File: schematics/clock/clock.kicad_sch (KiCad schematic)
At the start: 0 parts

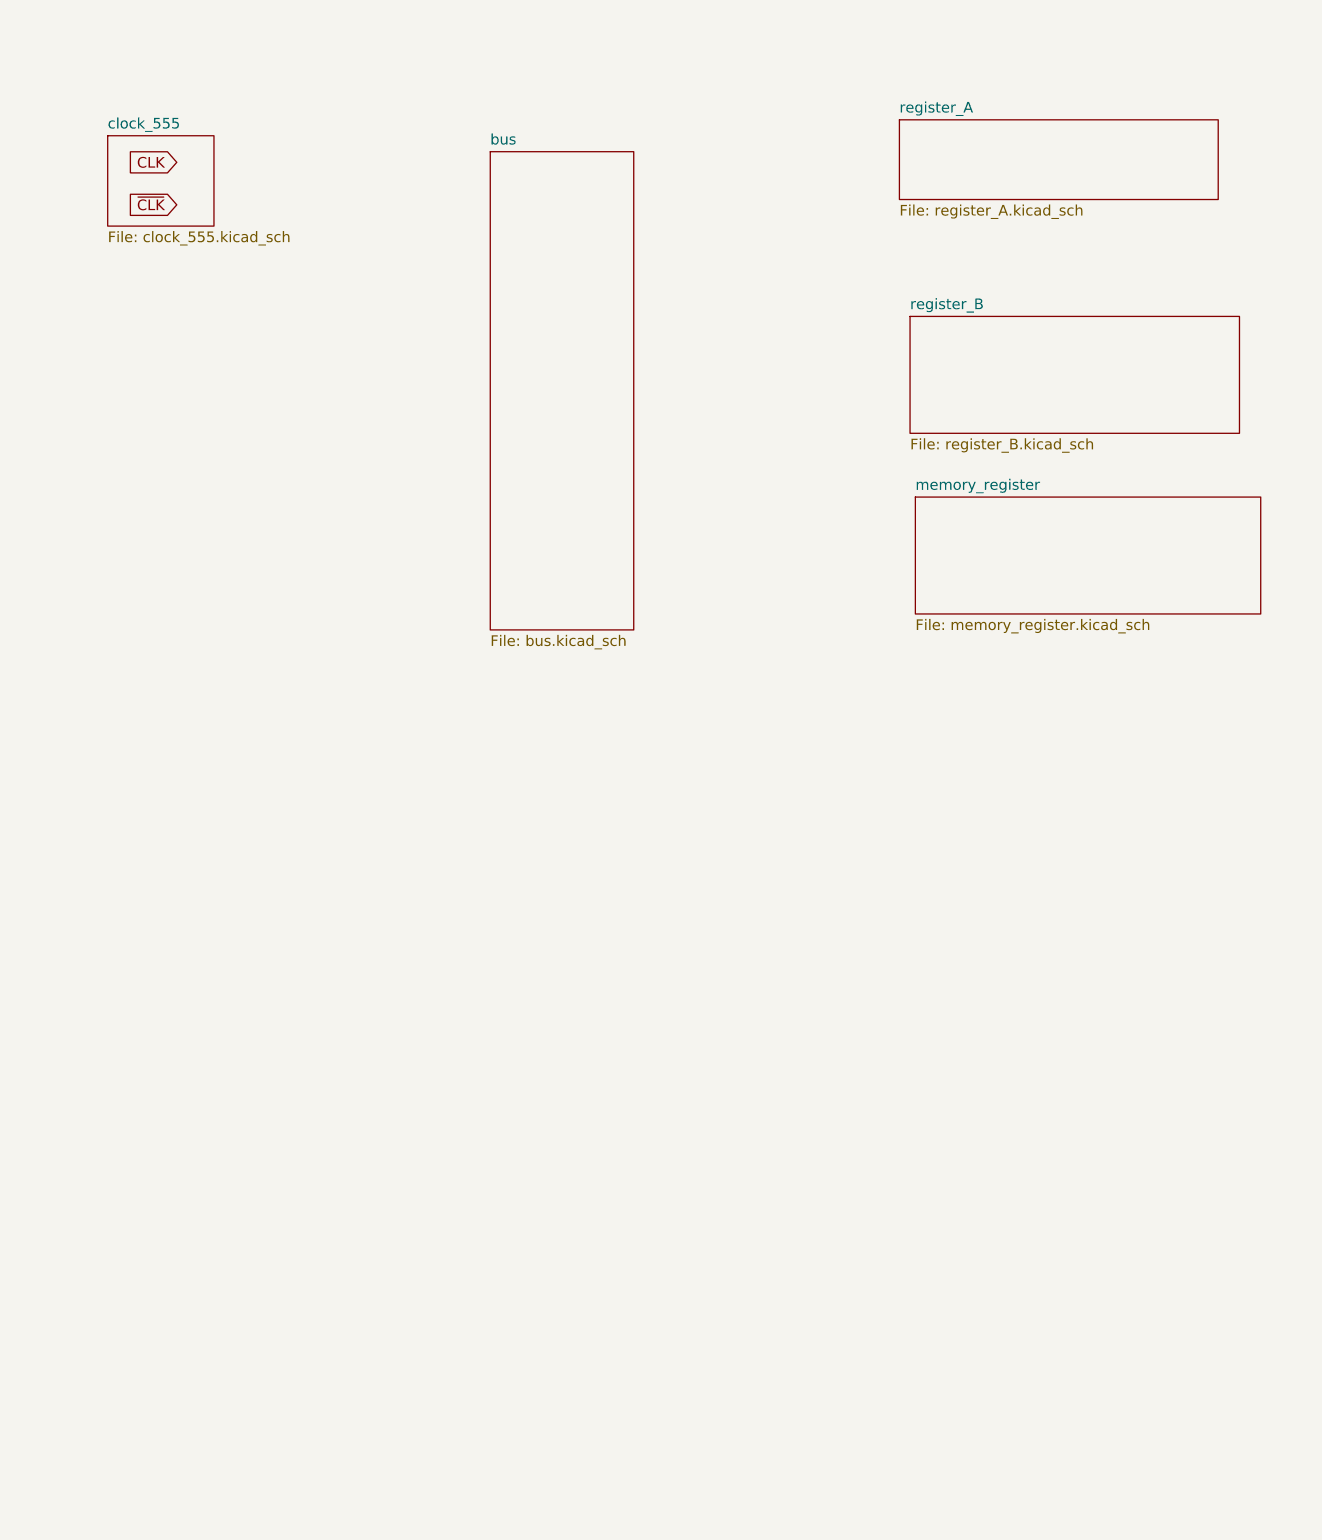
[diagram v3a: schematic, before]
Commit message: add bus
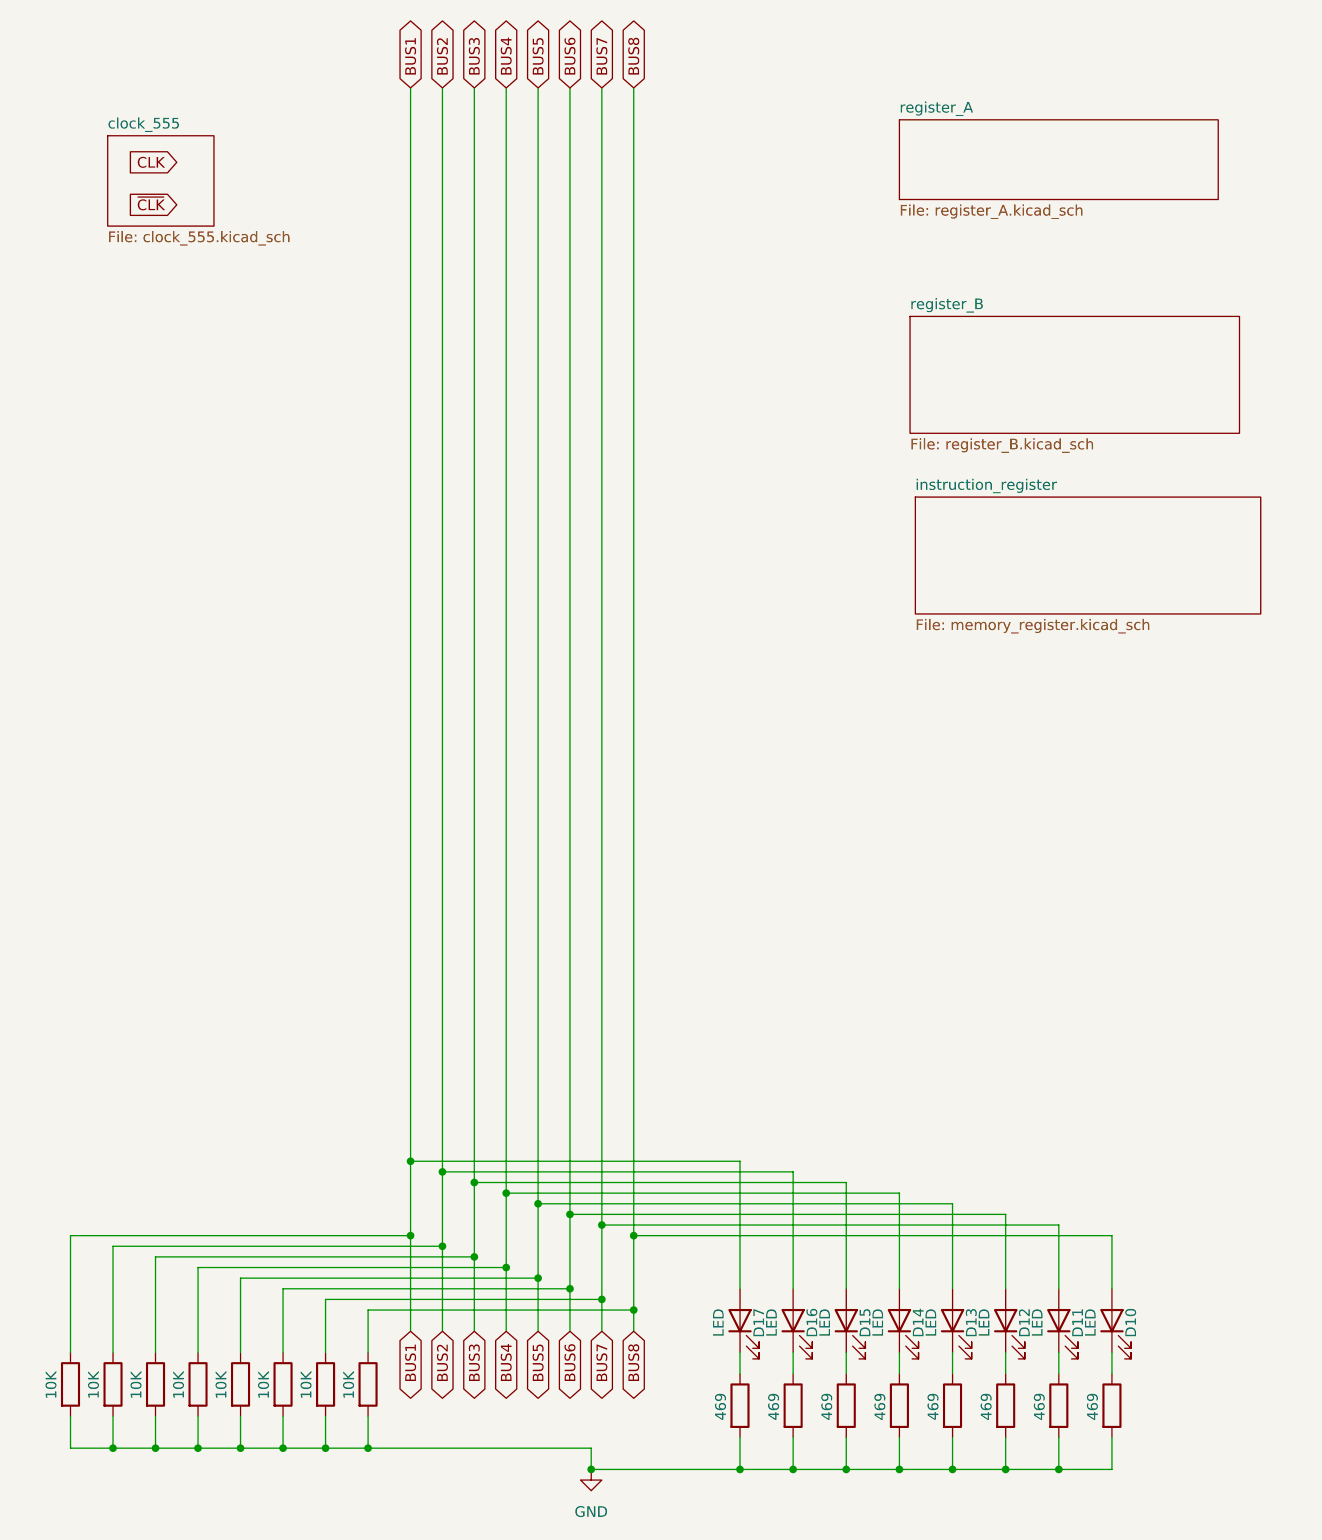
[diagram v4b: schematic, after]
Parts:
- added D10, D11, D12, D13, D14, D15, D16, D17: LED, symbol Device:LED
- added RLED10, RLED11, RLED12, RLED13, RLED14, RLED15, RLED16, RLED9: 469, symbol Device:R
- added RLED17, RLED18, RLED19, RLED20, RLED21, RLED22, RLED23, RLED24: 10K, symbol Device:R
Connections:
- new net: D12.1 (K), RLED11.1
- new net: D13.1 (K), RLED12.1
- new net: D11.1 (K), RLED10.1
- new net: D14.1 (K), RLED13.1
- new net: D10.1 (K), RLED9.1
- new net: D16.1 (K), RLED15.1
- new net: D15.1 (K), RLED14.1
- new net: D17.1 (K), RLED16.1
- new net BUS1: D17.2 (A), RLED23.1
- new net BUS2: D16.2 (A), RLED22.1
- new net BUS3: D15.2 (A), RLED21.1
- new net BUS4: D14.2 (A), RLED20.1
- new net BUS5: D13.2 (A), RLED19.1
- new net BUS6: D12.2 (A), RLED18.1
- new net BUS7: D11.2 (A), RLED17.1
- new net BUS8: D10.2 (A), RLED24.1
- new net GND: RLED10.2, RLED11.2, RLED12.2, RLED13.2, RLED14.2, RLED15.2, RLED16.2, RLED17.2, RLED18.2, RLED19.2, RLED20.2, RLED21.2, RLED22.2, RLED23.2, RLED24.2, RLED9.2
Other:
- sheet memory_register renamed instruction_register
- removed sheet bus

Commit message: change direction of bus
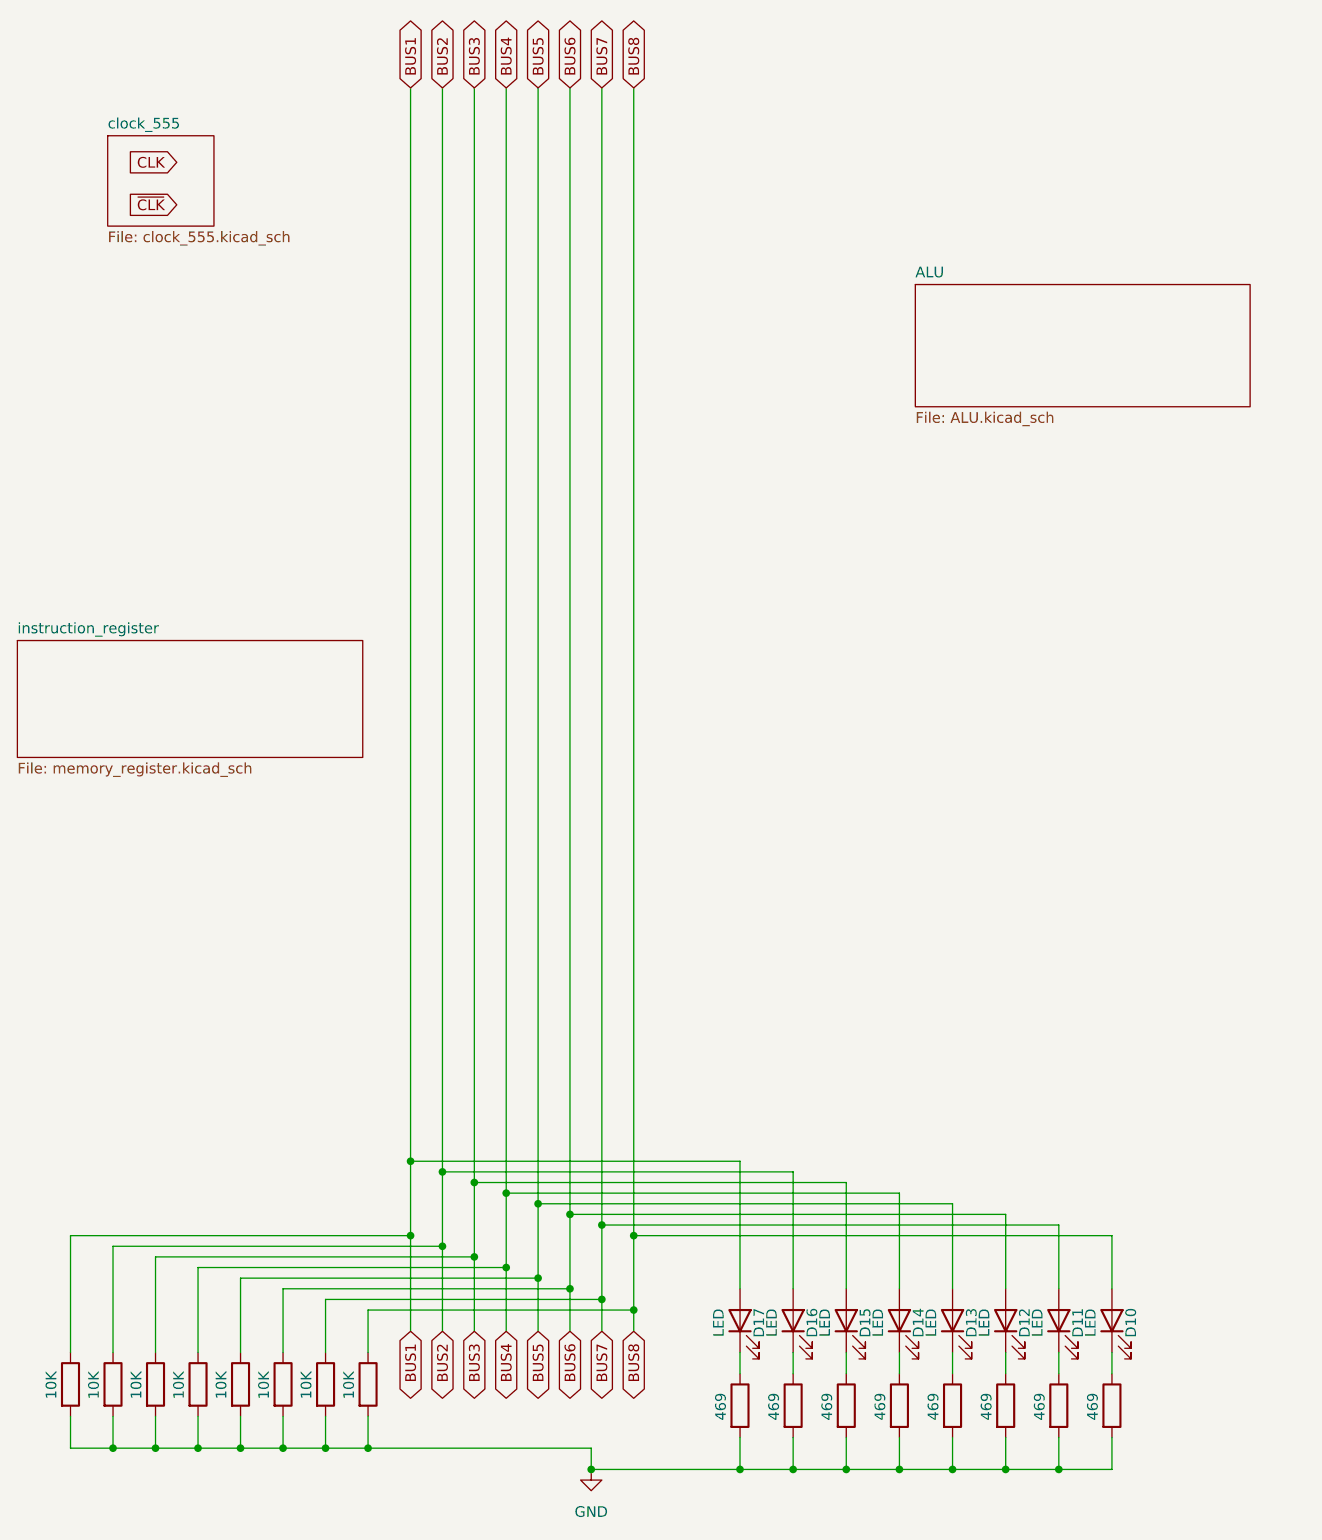
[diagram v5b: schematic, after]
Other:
- removed sheet register_A
- removed sheet register_B
- added sheet ALU (ALU.kicad_sch)
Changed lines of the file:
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@@
 	)
 	(sheet
-		(at 139.065 78.105)
+		(at 31.75 95.25)
 		(size 41.275 13.97)
 		(exclude_from_sim no)
@@
 		)
 		(property "Sheetname" "instruction_register"
-			(at 139.065 77.3934 0)
+			(at 31.75 94.5384 0)
 			(effects
 				(font
@@
 		)
 		(property "Sheetfile" "memory_register.kicad_sch"
-			(at 139.065 92.6596 0)
+			(at 31.75 109.8046 0)
 			(effects
 				(font
@@
 				(path "/1be175cd-1437-4d72-8152-541f02e1a99b"
 					(page "9")
-				)
-			)
-		)
-	)
-	(sheet
-		(at 138.43 56.515)
-		(size 39.37 13.97)
-		(exclude_from_sim no)
-		(in_bom yes)
-		(on_board yes)
-		(dnp no)
-		(fields_autoplaced yes)
-		(stroke
-			(width 0.1524)
-			(type solid)
-		)
-		(fill
-			(color 0 0 0 0.0000)
-		)
-		(property "Sheetname" "register_B"
-			(at 138.43 55.8034 0)
-			(effects
-				(font
-					(size 1.27 1.27)
-				)
-				(justify left bottom)
-			)
-		)
-		(property "Sheetfile" "register_B.kicad_sch"
-			(at 138.43 71.0696 0)
-			(effects
-				(font
-					(size 1.27 1.27)
-				)
-				(justify left top)
-			)
-		)
-		(instances
-			(project "clock"
-				(path "/1be175cd-1437-4d72-8152-541f02e1a99b"
-					(page "8")
 				)
 			)
@@
 	)
 	(sheet
-		(at 137.16 33.02)
-		(size 38.1 9.525)
+		(at 139.065 52.705)
+		(size 40.005 14.605)
 		(exclude_from_sim no)
 		(in_bom yes)
@@
 			(color 0 0 0 0.0000)
 		)
-		(property "Sheetname" "register_A"
-			(at 137.16 32.3084 0)
+		(property "Sheetname" "ALU"
+			(at 139.065 51.9934 0)
 			(effects
 				(font
@@
 			)
 		)
-		(property "Sheetfile" "register_A.kicad_sch"
-			(at 137.16 43.1296 0)
+		(property "Sheetfile" "ALU.kicad_sch"
+			(at 139.065 67.8946 0)
 			(effects
 				(font
@@
 			(project "clock"
 				(path "/1be175cd-1437-4d72-8152-541f02e1a99b"
-					(page "3")
+					(page "9")
 				)
 			)

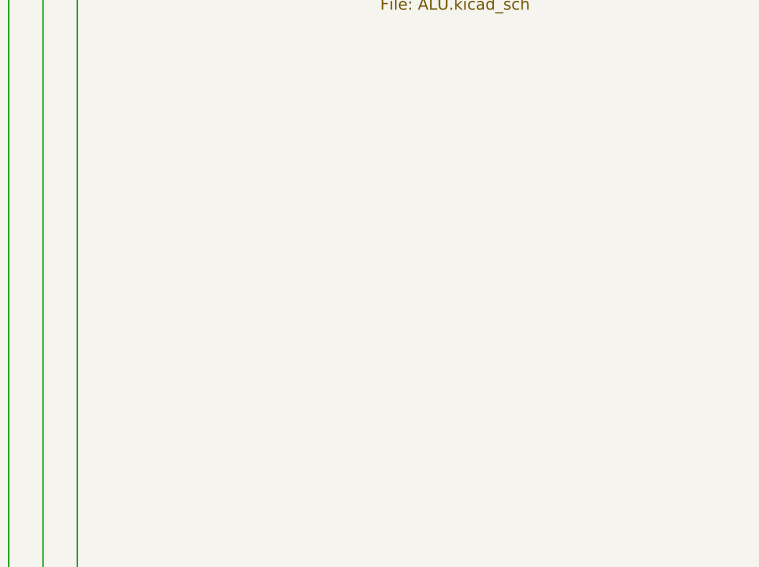
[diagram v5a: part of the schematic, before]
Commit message: add ram, change bus
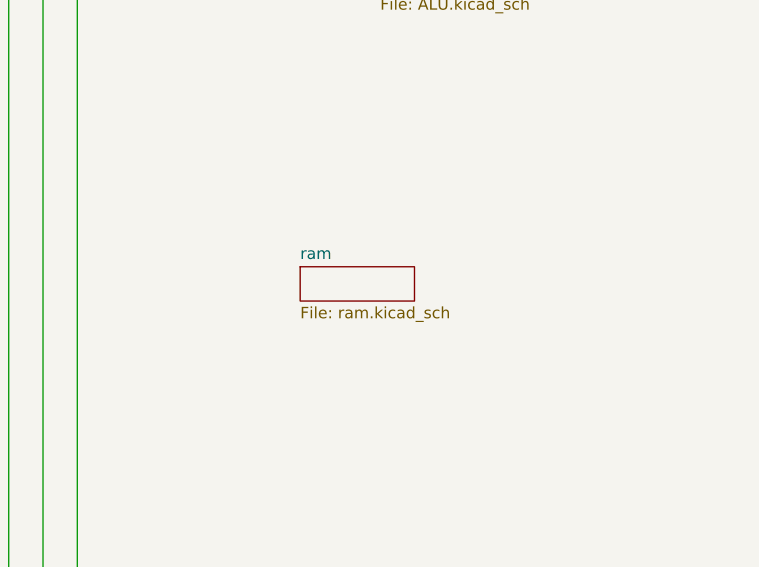
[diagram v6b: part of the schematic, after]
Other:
- added sheet ram (ram.kicad_sch)
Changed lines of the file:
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@@
+	)
+	(sheet
+		(at 130.175 97.79)
+		(size 12.7 3.81)
+		(exclude_from_sim no)
+		(in_bom yes)
+		(on_board yes)
+		(dnp no)
+		(fields_autoplaced yes)
+		(stroke
+			(width 0.1524)
+			(type solid)
+		)
+		(fill
+			(color 0 0 0 0.0000)
+		)
+		(property "Sheetname" "ram"
+			(at 130.175 97.0784 0)
+			(effects
+				(font
+					(size 1.27 1.27)
+				)
+				(justify left bottom)
+			)
+		)
+		(property "Sheetfile" "ram.kicad_sch"
+			(at 130.175 102.1846 0)
+			(effects
+				(font
+					(size 1.27 1.27)
+				)
+				(justify left top)
+			)
+		)
+		(instances
+			(project "clock"
+				(path "/1be175cd-1437-4d72-8152-541f02e1a99b"
+					(page "10")
+				)
+			)
+		)
 	)
 	(sheet
